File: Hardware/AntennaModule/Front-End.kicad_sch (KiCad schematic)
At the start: 24 parts, among them U1 C0727J5003AHF-1, U2 C0727J5003AHF-1, U3 NJG1155UX2, U4 NT1192FAAE1S, U5 PD0922J5050S2HF, U6 NT1192FAAE1S, X1 TA1985A, X2 TE0149A

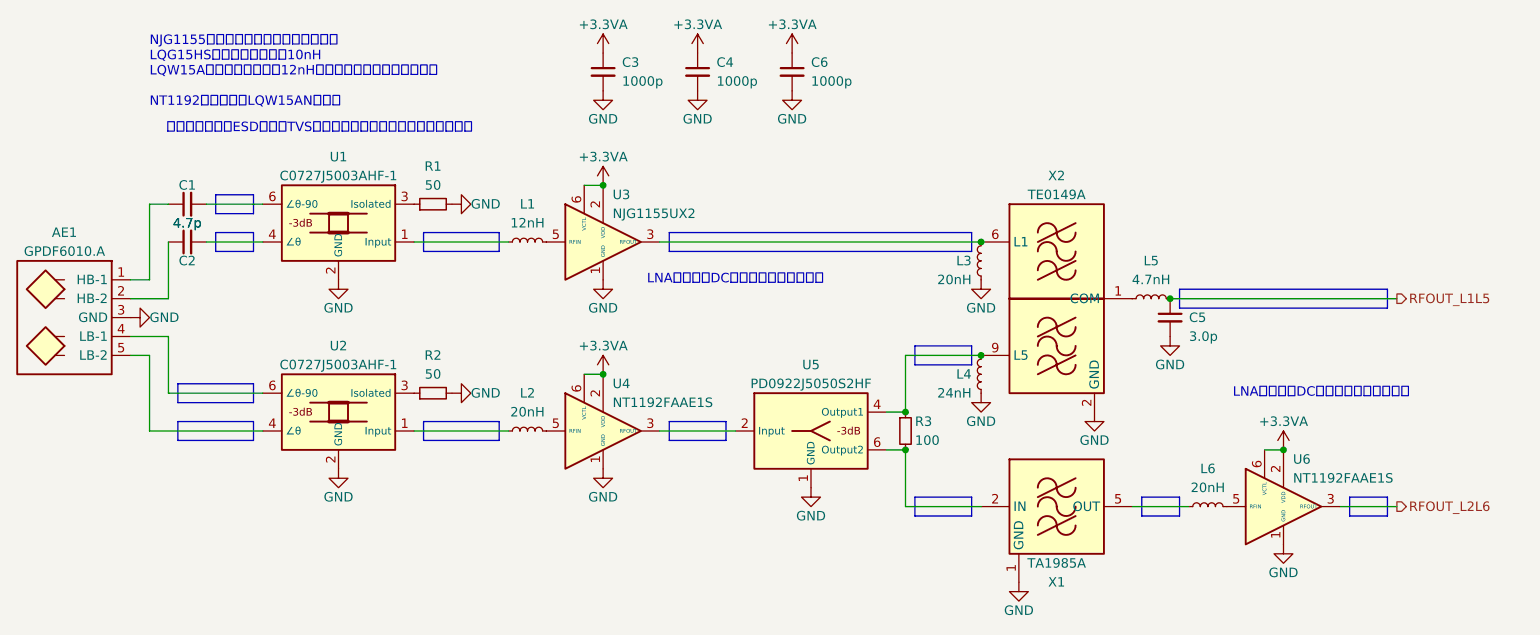
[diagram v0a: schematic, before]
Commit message: TE0149AをTE0133Bに変更
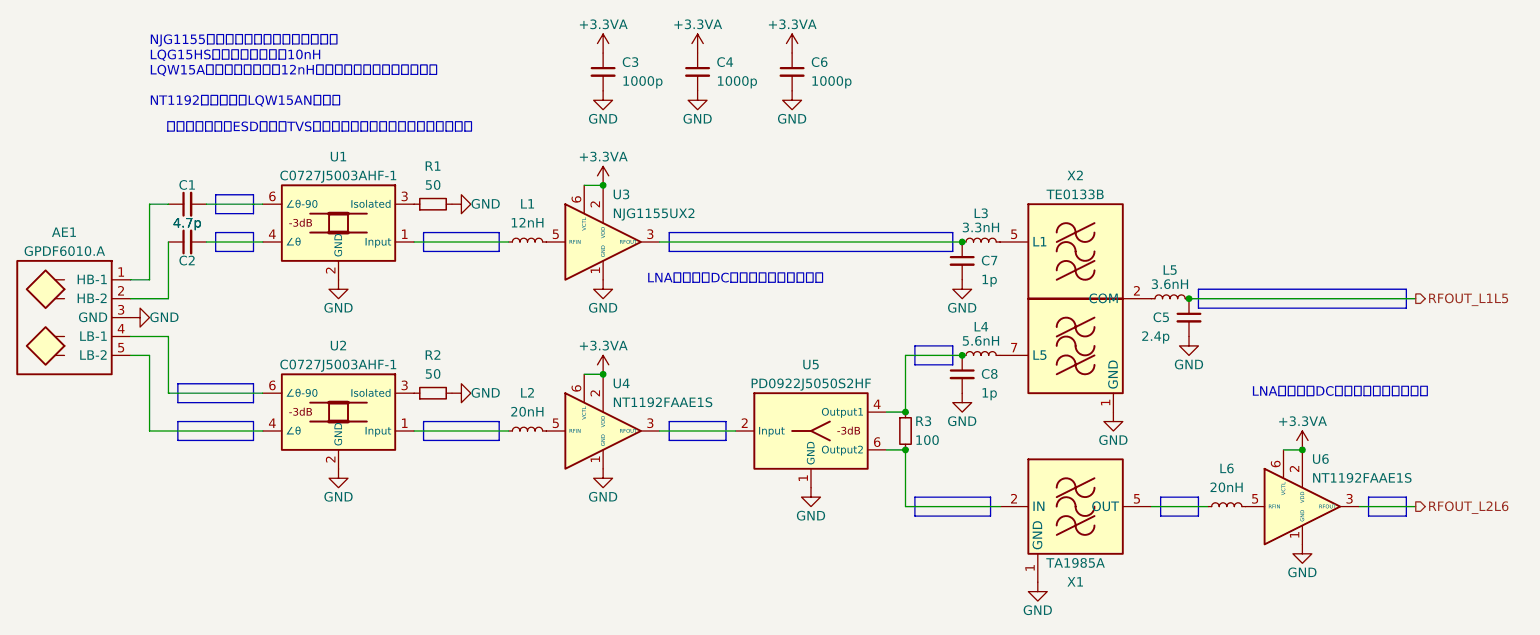
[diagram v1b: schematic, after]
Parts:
- removed X2: TE0149A, Filter_extlib:Filter_SAW-10_1.5x1.1mm, symbol Filter_extlib:TE0149A
- added C7, C8: 1p, symbol Device:C_Small
- added X2: TE0133B, Filter_extlib:Filter_SAW-8_3.0x3.0mm, symbol Filter_extlib:TE0133B
- C5: value 3.0p -> 2.4p
- L3: value 20nH -> 3.3nH
- L4: value 24nH -> 5.6nH
- L5: value 4.7nH -> 3.6nH
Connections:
- net GND: now also C7.2, C8.2, X2.1 (GND), X2.3 (GND), X2.4 (GND), X2.6 (GND), X2.8 (GND); no longer L3.2, L4.2
- net at L4.1, R3.1, U5.4 (Output1): now also C8.1
- net at L5.1: now also X2.2 (COM)
- net at L3.1, U3.3 (RFOUT): now also C7.1
- new net: L4.2, X2.7 (L5)
- new net: L3.2, X2.5 (L1)
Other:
- moved on the sheet: C5, L5, L6, U6, X1

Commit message: 回路図完成
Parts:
- removed AE1: GPDF6010.A, RF_Antenna_extlib:Taoglas_GPDF6010.A_GNSS, symbol RF_Antenna_extlib:GPDF6010.A
- added AE1, AE2: GPDF6010.A, RF_Antenna_extlib:Taoglas_GPDF6010.A_GNSS, symbol RF_Antenna_extlib:GPDF6010.A
- added D2, D3, D4, D5: AXGD10402KR, Diode_SMD_extlib:D_Littelfuse_AXGD10402KR_0402_1005Metric_1.02x0.51mm, symbol Device:D_TVS_Small
- C1, C2, C3, C4, C5, C6, C7, C8: footprint (none) -> Capacitor_SMD_extlib:C_Murata_xxx15_0402_1005Metric_1.0x0.5mm
- R3: footprint (none) -> Resistor_SMD_extlib:R_Vishay_FC0603xxxxxxTxx_0603_1608Metric_1.626x0.813mm
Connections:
- net GND: now also AE1.3 (GND), AE2.3 (GND), D2.2 (A2), D3.1 (A1), D4.2 (A2), D5.1 (A1)
- net at C2.1: now also AE2.2 (HB2), D2.1 (A1)
- net at C1.1: now also AE2.1 (HB1), D3.2 (A2)
- net at U2.6 (∠θ-90): now also AE1.4 (LB1), D5.2 (A2)
- net at U2.4 (∠θ): now also AE1.5 (LB2), D4.1 (A1)

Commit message: アンテナの給電点が逆になっていたのを修正
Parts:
- L1, L2, L3, L4, L5, L6: footprint (none) -> Inductor_SMD_extlib:L_Murata_LQW15ANxxxx80x_0402_1005Metric_1.0x0.6mm
- R1, R2: footprint (none) -> Resistor_SMD:R_0402_1005Metric
- renumbered AE2 to AE1
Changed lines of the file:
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@@
 			)
 		)
-		(property "Footprint" ""
+		(property "Footprint" "Inductor_SMD_extlib:L_Murata_LQW15ANxxxx80x_0402_1005Metric_1.0x0.6mm"
 			(at 213.36 129.54 0)
 			(effects
@@
 			)
 		)
-		(property "Footprint" ""
+		(property "Footprint" "Inductor_SMD_extlib:L_Murata_LQW15ANxxxx80x_0402_1005Metric_1.0x0.6mm"
 			(at 119.38 119.38 0)
 			(effects
@@
 			)
 		)
-		(property "Footprint" ""
+		(property "Footprint" "Inductor_SMD_extlib:L_Murata_LQW15ANxxxx80x_0402_1005Metric_1.0x0.6mm"
 			(at 180.34 109.22 0)
 			(effects
@@
 			)
 		)
-		(property "Footprint" ""
+		(property "Footprint" "Inductor_SMD_extlib:L_Murata_LQW15ANxxxx80x_0402_1005Metric_1.0x0.6mm"
 			(at 180.34 93.98 0)
 			(effects
@@
 			)
 		)
-		(property "Footprint" ""
+		(property "Footprint" "Inductor_SMD_extlib:L_Murata_LQW15ANxxxx80x_0402_1005Metric_1.0x0.6mm"
 			(at 119.38 93.98 0)
 			(effects
@@
 			)
 		)
-		(property "Footprint" ""
+		(property "Footprint" "Inductor_SMD_extlib:L_Murata_LQW15ANxxxx80x_0402_1005Metric_1.0x0.6mm"
 			(at 205.74 101.6 0)
 			(effects
@@
 		(dnp no)
 		(fields_autoplaced yes)
-		(property "Reference" "AE2"
+		(property "Reference" "AE1"
 			(at 58.42 81.28 0)
 			(effects
@@
 			(project ""
 				(path "/6fea4726-6625-4d37-9d0c-c1a5d08d59ce/6a1a8a49-81e8-4900-a7b3-937741017566"
-					(reference "AE2")
+					(reference "AE1")
 					(unit 1)
 				)
@@
 			)
 		)
-		(property "Footprint" ""
+		(property "Footprint" "Resistor_SMD:R_0402_1005Metric"
 			(at 106.68 114.3 0)
 			(effects
@@
 			)
 		)
-		(property "Footprint" ""
+		(property "Footprint" "Resistor_SMD:R_0402_1005Metric"
 			(at 106.68 88.9 0)
 			(effects

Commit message: アンテナのFP修正に伴う回路図の修正
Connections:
- net GND: now also AE1.5 (GND), AE1.5 (GND); no longer AE1.3 (GND), AE1.3 (GND)
- net at D4.1 (A1), U2.4 (∠θ): now also AE1.4 (LB2); no longer AE1.5 (LB2)
- net at D5.2 (A2), U2.6 (∠θ-90): now also AE1.3 (LB1); no longer AE1.4 (LB1)
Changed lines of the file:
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@@
 	)
 	(junction
+		(at 66.04 119.38)
+		(diameter 0)
+		(color 0 0 0 0)
+	)
+	(junction
 		(at 68.58 88.9)
 		(diameter 0)
@@
 	)
 	(junction
-		(at 177.8 109.22)
+		(at 66.04 93.98)
 		(diameter 0)
 		(color 0 0 0 0)
 	)
 	(junction
-		(at 66.04 93.98)
+		(at 177.8 109.22)
 		(diameter 0)
 		(color 0 0 0 0)
@@
 		(color 0 0 0 0)
 	)
-	(junction
-		(at 66.04 119.38)
-		(diameter 0)
-		(color 0 0 0 0)
-	)
 	(wire
 		(pts
@@
 	)
 	(symbol
+		(lib_id "RF_Antenna_extlib:GPDF6010.A")
+		(at 58.42 116.84 0)
+		(unit 2)
+		(exclude_from_sim no)
+		(in_bom yes)
+		(on_board yes)
+		(dnp no)
+		(fields_autoplaced yes)
+		(property "Reference" "AE1"
+			(at 58.42 106.68 0)
+			(effects
+				(font
+					(size 1.27 1.27)
+				)
+			)
+		)
+		(property "Value" "GPDF6010.A"
+			(at 58.42 109.22 0)
+			(effects
+				(font
+					(size 1.27 1.27)
+				)
+			)
+		)
+		(property "Footprint" "RF_Antenna_extlib:Taoglas_GPDF6010.A_GNSS"
+			(at 58.42 127 0)
+			(effects
+				(font
+					(size 1.27 1.27)
+				)
+				(hide yes)
+			)
+		)
+		(property "Datasheet" "https://www.taoglas.com/datasheets/GPDF6010.A.pdf"
+			(at 58.42 129.54 0)
+			(effects
+				(font
+					(size 1.27 1.27)
+				)
+				(hide yes)
+			)
+		)
+		(property "Description" "Passive All-band High Precision GNSS Stacked Dual Pin Dual Feed Patch Antenna"
+			(at 58.42 132.08 0)
+			(effects
+				(font
+					(size 1.27 1.27)
+				)
+				(hide yes)
+			)
+		)
+		(pin "5"
+		)
+		(pin "1"
+		)
+		(pin "2"
+		)
+		(pin "4"
+		)
+		(pin "3"
+		)
+		(pin "5"
+		)
+		(instances
+			(project ""
+				(path "/6fea4726-6625-4d37-9d0c-c1a5d08d59ce/6a1a8a49-81e8-4900-a7b3-937741017566"
+					(reference "AE1")
+					(unit 2)
+				)
+			)
+		)
+	)
+	(symbol
 		(lib_id "power:+3.3VA")
 		(at 154.94 68.58 0)
@@
 	)
 	(symbol
-		(lib_name "GPDF6010.A_1")
-		(lib_id "RF_Antenna_extlib:GPDF6010.A")
-		(at 58.42 91.44 0)
-		(unit 1)
-		(exclude_from_sim no)
-		(in_bom yes)
-		(on_board yes)
-		(dnp no)
-		(fields_autoplaced yes)
-		(property "Reference" "AE1"
-			(at 58.42 81.28 0)
-			(effects
-				(font
-					(size 1.27 1.27)
-				)
-			)
-		)
-		(property "Value" "GPDF6010.A"
-			(at 58.42 83.82 0)
-			(effects
-				(font
-					(size 1.27 1.27)
-				)
-			)
-		)
-		(property "Footprint" "RF_Antenna_extlib:Taoglas_GPDF6010.A_GNSS"
-			(at 58.42 101.6 0)
-			(effects
-				(font
-					(size 1.27 1.27)
-				)
-				(hide yes)
-			)
-		)
-		(property "Datasheet" "https://www.taoglas.com/datasheets/GPDF6010.A.pdf"
-			(at 58.42 104.14 0)
-			(effects
-				(font
-					(size 1.27 1.27)
-				)
-				(hide yes)
-			)
-		)
-		(property "Description" "Passive All-band High Precision GNSS Stacked Dual Pin Dual Feed Patch Antenna"
-			(at 58.42 106.68 0)
-			(effects
-				(font
-					(size 1.27 1.27)
-				)
-				(hide yes)
-			)
-		)
-		(pin "2"
-		)
-		(pin "5"
-		)
-		(pin "1"
-		)
-		(pin "3"
-		)
-		(pin "3"
-		)
-		(pin "4"
-		)
-		(instances
-			(project ""
-				(path "/6fea4726-6625-4d37-9d0c-c1a5d08d59ce/6a1a8a49-81e8-4900-a7b3-937741017566"
-					(reference "AE1")
-					(unit 1)
-				)
-			)
-		)
-	)
-	(symbol
 		(lib_id "Device:C_Small")
 		(at 142.24 71.12 0)
@@
 	)
 	(symbol
-		(lib_name "GPDF6010.A_1")
-		(lib_id "RF_Antenna_extlib:GPDF6010.A")
-		(at 58.42 116.84 0)
-		(unit 2)
-		(exclude_from_sim no)
-		(in_bom yes)
-		(on_board yes)
-		(dnp no)
-		(property "Reference" "AE1"
-			(at 58.42 106.68 0)
-			(effects
-				(font
-					(size 1.27 1.27)
-				)
-			)
-		)
-		(property "Value" "GPDF6010.A"
-			(at 58.42 109.22 0)
-			(effects
-				(font
-					(size 1.27 1.27)
-				)
-			)
-		)
-		(property "Footprint" "RF_Antenna_extlib:Taoglas_GPDF6010.A_GNSS"
-			(at 58.42 127 0)
-			(effects
-				(font
-					(size 1.27 1.27)
-				)
-				(hide yes)
-			)
-		)
-		(property "Datasheet" "https://www.taoglas.com/datasheets/GPDF6010.A.pdf"
-			(at 58.42 129.54 0)
-			(effects
-				(font
-					(size 1.27 1.27)
-				)
-				(hide yes)
-			)
-		)
-		(property "Description" "Passive All-band High Precision GNSS Stacked Dual Pin Dual Feed Patch Antenna"
-			(at 58.42 132.08 0)
-			(effects
-				(font
-					(size 1.27 1.27)
-				)
-				(hide yes)
-			)
-		)
-		(pin "2"
-		)
-		(pin "5"
-		)
-		(pin "1"
-		)
-		(pin "3"
-		)
-		(pin "3"
-		)
-		(pin "4"
-		)
-		(instances
-			(project ""
-				(path "/6fea4726-6625-4d37-9d0c-c1a5d08d59ce/6a1a8a49-81e8-4900-a7b3-937741017566"
-					(reference "AE1")
-					(unit 2)
-				)
-			)
-		)
-	)
-	(symbol
 		(lib_id "power:+3.3VA")
 		(at 142.24 68.58 0)
@@
 					(unit 1)
 				)
+			)
+		)
+	)
+	(symbol
+		(lib_id "RF_Antenna_extlib:GPDF6010.A")
+		(at 58.42 91.44 0)
+		(unit 1)
+		(exclude_from_sim no)
+		(in_bom yes)
+		(on_board yes)
+		(dnp no)
+		(fields_autoplaced yes)
+		(property "Reference" "AE1"
+			(at 58.42 81.28 0)
+			(effects
+				(font
+					(size 1.27 1.27)
+				)
+			)
+		)
+		(property "Value" "GPDF6010.A"
+			(at 58.42 83.82 0)
+			(effects
+				(font
+					(size 1.27 1.27)
+				)
+			)
+		)
+		(property "Footprint" "RF_Antenna_extlib:Taoglas_GPDF6010.A_GNSS"
+			(at 58.42 101.6 0)
+			(effects
+				(font
+					(size 1.27 1.27)
+				)
+				(hide yes)
+			)
+		)
+		(property "Datasheet" "https://www.taoglas.com/datasheets/GPDF6010.A.pdf"
+			(at 58.42 104.14 0)
+			(effects
+				(font
+					(size 1.27 1.27)
+				)
+				(hide yes)
+			)
+		)
+		(property "Description" "Passive All-band High Precision GNSS Stacked Dual Pin Dual Feed Patch Antenna"
+			(at 58.42 106.68 0)
+			(effects
+				(font
+					(size 1.27 1.27)
+				)
+				(hide yes)
+			)
+		)
+		(pin "5"
+		)
+		(pin "1"
+		)
+		(pin "2"
+		)
+		(pin "4"
+		)
+		(pin "3"
+		)
+		(pin "5"
+		)
+		(instances
+			(project ""
+				(path "/6fea4726-6625-4d37-9d0c-c1a5d08d59ce/6a1a8a49-81e8-4900-a7b3-937741017566"
+					(reference "AE1")
+					(unit 1)
+				)

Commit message: 部品配置決定
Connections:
- net at C8.1, L4.1, R3.1: now also U5.6 (Output2); no longer U5.4 (Output1)
- net at R3.2, X1.2 (IN): now also U5.4 (Output1); no longer U5.6 (Output2)
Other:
- note added: "パワーディバイダの接続は必要に応じて逆にする ハイブリッドカプラも反転可能"
- moved on the sheet: U5
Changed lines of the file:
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@@
 	)
 	(junction
-		(at 170.18 116.84)
-		(diameter 0)
-		(color 0 0 0 0)
-	)
-	(junction
 		(at 66.04 119.38)
 		(diameter 0)
@@
 	)
 	(junction
-		(at 170.18 121.92)
+		(at 170.18 116.84)
 		(diameter 0)
 		(color 0 0 0 0)
@@
 	)
 	(junction
+		(at 170.18 121.92)
+		(diameter 0)
+		(color 0 0 0 0)
+	)
+	(junction
 		(at 129.54 111.76)
 		(diameter 0)
@@
 	(wire
 		(pts
-			(xy 167.64 121.92) (xy 170.18 121.92)
+			(xy 66.04 88.9) (xy 68.58 88.9)
 		)
 		(stroke
@@
 	(wire
 		(pts
-			(xy 66.04 88.9) (xy 68.58 88.9)
+			(xy 167.64 121.92) (xy 170.18 121.92)
 		)
 		(stroke
@@
 	(wire
 		(pts
-			(xy 127 111.76) (xy 129.54 111.76)
+			(xy 167.64 116.84) (xy 170.18 116.84)
 		)
 		(stroke
@@
 	(wire
 		(pts
-			(xy 66.04 93.98) (xy 71.12 93.98)
+			(xy 127 111.76) (xy 129.54 111.76)
 		)
 		(stroke
@@
 	(wire
 		(pts
-			(xy 76.2 88.9) (xy 83.82 88.9)
+			(xy 66.04 93.98) (xy 71.12 93.98)
 		)
 		(stroke
@@
 	(wire
 		(pts
-			(xy 104.14 93.98) (xy 116.84 93.98)
+			(xy 76.2 88.9) (xy 83.82 88.9)
 		)
 		(stroke
@@
 	(wire
 		(pts
-			(xy 76.2 93.98) (xy 83.82 93.98)
+			(xy 104.14 93.98) (xy 116.84 93.98)
 		)
 		(stroke
@@
 	(wire
 		(pts
-			(xy 220.98 121.92) (xy 223.52 121.92)
+			(xy 76.2 93.98) (xy 83.82 93.98)
 		)
 		(stroke
@@
 	(wire
 		(pts
-			(xy 167.64 116.84) (xy 170.18 116.84)
+			(xy 220.98 121.92) (xy 223.52 121.92)
 		)
 		(stroke
@@
 		)
 	)
+	(text "パワーディバイダの接続は必要に応じて逆にする\nハイブリッドカプラも反転可能"
+		(exclude_from_sim no)
+		(at 55.88 137.16 0)
+		(effects
+			(font
+				(size 1.27 1.27)
+			)
+			(justify left top)
+		)
+	)
 	(text "アンテナからのESD対策にTVSダイオードが必要なのかどうか考える"
 		(exclude_from_sim no)
@@
 		(lib_id "RF_Converter_extlib:PD0922J5050S2HF")
 		(at 157.48 119.38 0)
+		(mirror x)
 		(unit 1)
 		(exclude_from_sim no)
@@
 		(dnp no)
 		(property "Reference" "U5"
-			(at 157.48 110.49 0)
+			(at 157.48 128.27 0)
 			(effects
 				(font
@@
 		)
 		(property "Value" "PD0922J5050S2HF"
-			(at 157.48 113.03 0)
+			(at 157.48 125.73 0)
 			(effects
 				(font
@@
 		)
 		(property "Footprint" "RF_Converter_extlib:Xinger_0805_2012Metric-6_Pad0.33x0.41mm"
-			(at 157.48 134.62 0)
+			(at 157.48 104.14 0)
 			(effects
 				(font
@@
 		)
 		(property "Datasheet" "https://cdn.ttm.com/repository/products/wireless-xinger/power-dividers/PD0922J5050S2HF/PD0922J5050S2HF.pdf"
-			(at 157.48 137.16 0)
+			(at 157.48 101.6 0)
 			(effects
 				(font
@@
 		)
 		(property "Description" "0.95-2.15GHz Wilkinson Power Divider, Xinger 0805"
-			(at 157.48 139.7 0)
+			(at 157.48 99.06 0)
 			(effects
 				(font
@@
 	(symbol
 		(lib_id "power:GND")
-		(at 157.48 127 0)
+		(at 157.48 111.76 180)
 		(unit 1)
 		(exclude_from_sim no)
@@
 		(dnp no)
 		(property "Reference" "#PWR014"
-			(at 157.48 133.35 0)
+			(at 157.48 105.41 0)
 			(effects
 				(font
@@
 		)
 		(property "Value" "GND"
-			(at 157.48 130.81 0)
+			(at 157.48 107.95 0)
 			(effects
 				(font
@@
 		)
 		(property "Footprint" ""
-			(at 157.48 127 0)
+			(at 157.48 111.76 0)
 			(effects
 				(font
@@
 		)
 		(property "Datasheet" ""
-			(at 157.48 127 0)
+			(at 157.48 111.76 0)
 			(effects
 				(font
@@
 		)
 		(property "Description" "Power symbol creates a global label with name \"GND\" , ground"
-			(at 157.48 127 0)
+			(at 157.48 111.76 0)
 			(effects
 				(font
